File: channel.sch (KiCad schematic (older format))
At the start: 7 parts, among them Q1 MMBT5551, Q2 SiS402DN, Q3 MMBT5401

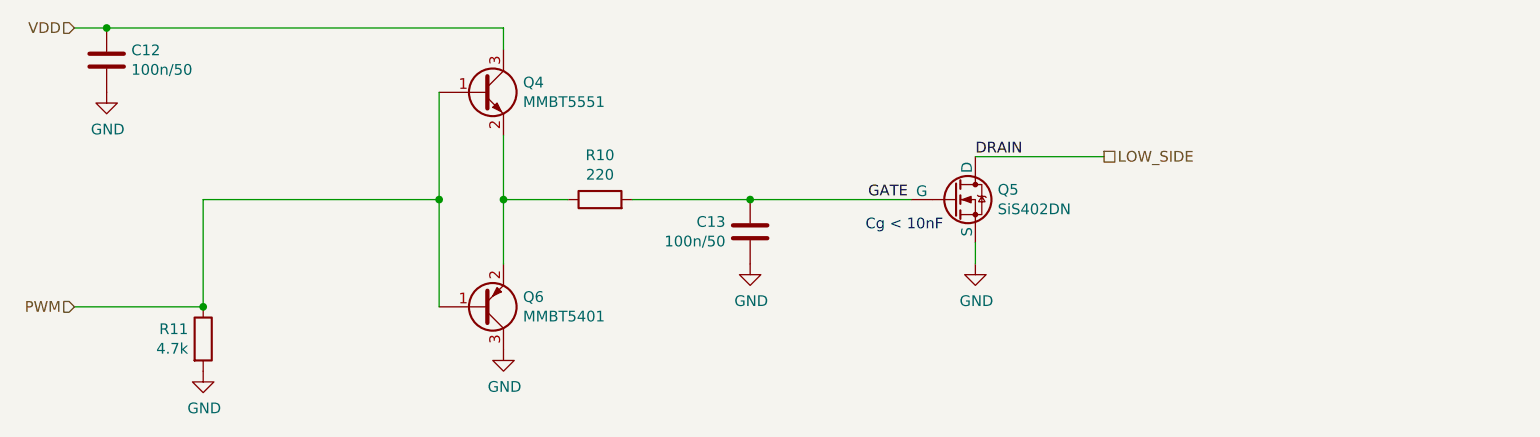
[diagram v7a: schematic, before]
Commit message: add mosfets, fix led+i2c resistors
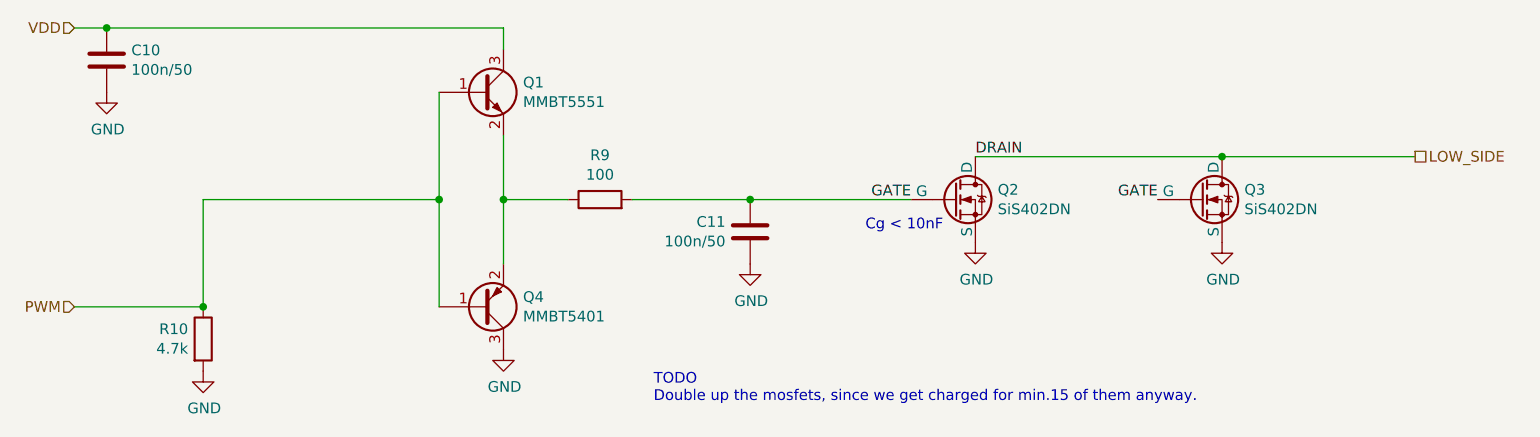
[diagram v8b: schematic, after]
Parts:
- added Q3: SiS402DN, Package_SO:Vishay_PowerPAK_1212-8_Single, symbol mark:SiS402DN
- Q2: JLC (none) -> C15791
- R9: renamed from R8; value 220 -> 100; JLC C25091 -> C25076
- renumbered Q3 to Q4, R9 to R10
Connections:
- net GATE: now also Q3.4 (G)
- net GND: now also Q3.1 (S), Q3.2 (S), Q3.3 (S)
- net LOW_SIDE: now also Q3.5 (D)
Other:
- note added: "TODO\nDouble up the mosfets, since we get charged for min.15 of them anyway."
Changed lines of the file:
@@
 AR Path="/61C031A1/61C0AE1D" Ref="#PWR?"  Part="1"
 AR Path="/61C031A3/61C0AE1D" Ref="#PWR?"  Part="1"
-AR Path="/6202E846/61C0AE1D" Ref="#PWR030"  Part="1"
-AR Path="/620593AE/61C0AE1D" Ref="#PWR035"  Part="1"
-F 0 "#PWR035" H 3000 2400 50  0001 C CNN
+AR Path="/6202E846/61C0AE1D" Ref="#PWR031"  Part="1"
+AR Path="/620593AE/61C0AE1D" Ref="#PWR037"  Part="1"
+F 0 "#PWR031" H 3000 2400 50  0001 C CNN
 F 1 "GND" H 3005 2477 50  0000 C CNN
 F 2 "" H 3000 2650 50  0001 C CNN
@@
 AR Path="/61C031A3/61C0ECF9" Ref="R?"  Part="1"
 AR Path="/61C0ECF9" Ref="R?"  Part="1"
-AR Path="/6202E846/61C0ECF9" Ref="R9"  Part="1"
-AR Path="/620593AE/61C0ECF9" Ref="R11"  Part="1"
-F 0 "R11" H 1530 2646 50  0000 R CNN
+AR Path="/6202E846/61C0ECF9" Ref="R10"  Part="1"
+AR Path="/620593AE/61C0ECF9" Ref="R12"  Part="1"
+F 0 "R10" H 1530 2646 50  0000 R CNN
 F 1 "4.7k" H 1530 2555 50  0000 R CNN
 F 2 "Resistor_SMD:R_0402_1005Metric" V 1530 2600 50  0001 C CNN
@@
 AR Path="/61C031A1/61C1051F" Ref="#PWR?"  Part="1"
 AR Path="/61C031A3/61C1051F" Ref="#PWR?"  Part="1"
-AR Path="/6202E846/61C1051F" Ref="#PWR031"  Part="1"
-AR Path="/620593AE/61C1051F" Ref="#PWR036"  Part="1"
-F 0 "#PWR036" H 1600 2500 50  0001 C CNN
+AR Path="/6202E846/61C1051F" Ref="#PWR032"  Part="1"
+AR Path="/620593AE/61C1051F" Ref="#PWR038"  Part="1"
+F 0 "#PWR032" H 1600 2500 50  0001 C CNN
 F 1 "GND" H 1605 2577 50  0000 C CNN
 F 2 "" H 1600 2750 50  0001 C CNN
@@
 P 2900 1450
 AR Path="/6202E846/61C0A1BB" Ref="Q1"  Part="1"
-AR Path="/620593AE/61C0A1BB" Ref="Q4"  Part="1"
-F 0 "Q4" H 3091 1496 50  0000 L CNN
+AR Path="/620593AE/61C0A1BB" Ref="Q5"  Part="1"
+F 0 "Q1" H 3091 1496 50  0000 L CNN
 F 1 "MMBT5551" H 3091 1405 50  0000 L CNN
 F 2 "Package_TO_SOT_SMD:SOT-23" H 3100 1375 50  0001 L CIN
@@
 AR Path="/61C031A3/61C5A1AF" Ref="R?"  Part="1"
 AR Path="/61C5A1AF" Ref="R?"  Part="1"
-AR Path="/6202E846/61C5A1AF" Ref="R8"  Part="1"
-AR Path="/620593AE/61C5A1AF" Ref="R10"  Part="1"
-F 0 "R10" V 3657 1950 50  0000 C CNN
-F 1 "220" V 3566 1950 50  0000 C CNN
+AR Path="/6202E846/61C5A1AF" Ref="R9"  Part="1"
+AR Path="/620593AE/61C5A1AF" Ref="R11"  Part="1"
+F 0 "R9" V 3657 1950 50  0000 C CNN
+F 1 "100" V 3566 1950 50  0000 C CNN
 F 2 "Resistor_SMD:R_0402_1005Metric_Pad0.72x0.64mm_HandSolder" V 3380 1950 50  0001 C CNN
 F 3 "~" H 3450 1950 50  0001 C CNN
-F 4 "C25091" H 3450 1950 50  0001 C CNN "JLC"
+F 4 "C25076" H 3450 1950 50  0001 C CNN "JLC"
 	1    3450 1950
 	0    -1   -1   0
@@
 	3000 1150 3000 1250
 $Comp
-L Device:Q_PNP_BEC Q3
+L Device:Q_PNP_BEC Q4
 U 1 1 61C4E023
 P 2900 2450
-AR Path="/6202E846/61C4E023" Ref="Q3"  Part="1"
-AR Path="/620593AE/61C4E023" Ref="Q6"  Part="1"
-F 0 "Q6" H 3091 2404 50  0000 L CNN
+AR Path="/6202E846/61C4E023" Ref="Q4"  Part="1"
+AR Path="/620593AE/61C4E023" Ref="Q8"  Part="1"
+F 0 "Q4" H 3091 2404 50  0000 L CNN
 F 1 "MMBT5401" H 3091 2495 50  0000 L CNN
 F 2 "Package_TO_SOT_SMD:SOT-23" H 3100 2550 50  0001 C CNN
@@
 AR Path="/6202E846/61D142B7" Ref="C10"  Part="1"
 AR Path="/620593AE/61D142B7" Ref="C12"  Part="1"
-F 0 "C12" H 1265 1346 50  0000 L CNN
+F 0 "C10" H 1265 1346 50  0000 L CNN
 F 1 "100n/50" H 1265 1255 50  0000 L CNN
 F 2 "Capacitor_SMD:C_0402_1005Metric" H 1188 1150 50  0001 C CNN
@@
 AR Path="/61C031A3/61D15BBF" Ref="#PWR?"  Part="1"
 AR Path="/6202E846/61D15BBF" Ref="#PWR027"  Part="1"
-AR Path="/620593AE/61D15BBF" Ref="#PWR032"  Part="1"
-F 0 "#PWR032" H 1150 1200 50  0001 C CNN
+AR Path="/620593AE/61D15BBF" Ref="#PWR033"  Part="1"
+F 0 "#PWR027" H 1150 1200 50  0001 C CNN
 F 1 "GND" H 1155 1277 50  0000 C CNN
 F 2 "" H 1150 1450 50  0001 C CNN
@@
 	4150 1950 4900 1950
 Wire Wire Line
-	5200 1750 5800 1750
+	5200 1750 6350 1750
 $Comp
 L mark:SiS402DN Q2
@@
 P 5100 1950
 AR Path="/6202E846/622D62B8" Ref="Q2"  Part="1"
-AR Path="/620593AE/622D62B8" Ref="Q5"  Part="1"
-F 0 "Q5" H 5304 1996 50  0000 L CNN
+AR Path="/620593AE/622D62B8" Ref="Q6"  Part="1"
+F 0 "Q2" H 5304 1996 50  0000 L CNN
 F 1 "SiS402DN" H 5304 1905 50  0000 L CNN
 F 2 "Package_SO:Vishay_PowerPAK_1212-8_Single" H 5100 2450 50  0001 C CNN
 F 3 "https://datasheet.lcsc.com/lcsc/1809301517_Vishay-Intertech-SIS402DN-T1-GE3_C15791.pdf" H 5100 1950 50  0001 C CNN
+F 4 "C15791" H 5100 1950 50  0001 C CNN "JLC"
 	1    5100 1950
 	1    0    0    -1
 $EndComp
-Text HLabel 5800 1750 2    50   UnSpc ~ 0
+Text HLabel 7250 1750 2    50   UnSpc ~ 0
 LOW_SIDE
 $Comp
 L power:GND #PWR?
 U 1 1 6203BB32
-P 5200 2250
+P 5200 2150
 AR Path="/61B5C5B6/6203BB32" Ref="#PWR?"  Part="1"
 AR Path="/61C03040/6203BB32" Ref="#PWR?"  Part="1"
@@
 AR Path="/61C031A3/6203BB32" Ref="#PWR?"  Part="1"
 AR Path="/6203BB32" Ref="#PWR?"  Part="1"
-AR Path="/6202E846/6203BB32" Ref="#PWR029"  Part="1"
+AR Path="/6202E846/6203BB32" Ref="#PWR028"  Part="1"
 AR Path="/620593AE/6203BB32" Ref="#PWR034"  Part="1"
-F 0 "#PWR034" H 5200 2000 50  0001 C CNN
-F 1 "GND" H 5205 2077 50  0000 C CNN
-F 2 "" H 5200 2250 50  0001 C CNN
-F 3 "" H 5200 2250 50  0001 C CNN
-	1    5200 2250
+F 0 "#PWR028" H 5200 1900 50  0001 C CNN
+F 1 "GND" H 5205 1977 50  0000 C CNN
+F 2 "" H 5200 2150 50  0001 C CNN
+F 3 "" H 5200 2150 50  0001 C CNN
+	1    5200 2150
 	1    0    0    -1
 $EndComp
 Text Label 5200 1750 0    50   ~ 0
 DRAIN
-Text Label 4700 1950 0    50   ~ 0
+Text Label 4900 1950 2    50   ~ 0
 GATE
-Wire Wire Line
-	5200 2250 5200 2150
 Connection ~ 4150 1950
 Wire Wire Line
@@
 AR Path="/6202E846/61C61D09" Ref="C11"  Part="1"
 AR Path="/620593AE/61C61D09" Ref="C13"  Part="1"
-F 0 "C13" H 4035 2146 50  0000 R CNN
+F 0 "C11" H 4035 2146 50  0000 R CNN
 F 1 "100n/50" H 4035 2055 50  0000 R CNN
 F 2 "Capacitor_SMD:C_0402_1005Metric_Pad0.74x0.62mm_HandSolder" H 4188 1950 50  0001 C CNN
@@
 AR Path="/61C031A1/61C20664" Ref="#PWR?"  Part="1"
 AR Path="/61C031A3/61C20664" Ref="#PWR?"  Part="1"
-AR Path="/6202E846/61C20664" Ref="#PWR028"  Part="1"
-AR Path="/620593AE/61C20664" Ref="#PWR033"  Part="1"
-F 0 "#PWR033" H 4150 2000 50  0001 C CNN
+AR Path="/6202E846/61C20664" Ref="#PWR030"  Part="1"
+AR Path="/620593AE/61C20664" Ref="#PWR036"  Part="1"
+F 0 "#PWR030" H 4150 2000 50  0001 C CNN
 F 1 "GND" H 4155 2077 50  0000 C CNN
 F 2 "" H 4150 2250 50  0001 C CNN
@@
 	1    0    0    -1
 $EndComp
+Text Notes 3700 2900 0    50   ~ 0
+TODO\nDouble up the mosfets, since we get charged for min.15 of them anyway.
+$Comp
+L mark:SiS402DN Q3
+U 1 1 6236D64F
+P 6250 1950
+AR Path="/6202E846/6236D64F" Ref="Q3"  Part="1"
+AR Path="/620593AE/6236D64F" Ref="Q7"  Part="1"
+F 0 "Q3" H 6454 1996 50  0000 L CNN
+F 1 "SiS402DN" H 6454 1905 50  0000 L CNN
+F 2 "Package_SO:Vishay_PowerPAK_1212-8_Single" H 6250 2450 50  0001 C CNN
+F 3 "https://datasheet.lcsc.com/lcsc/1809301517_Vishay-Intertech-SIS402DN-T1-GE3_C15791.pdf" H 6250 1950 50  0001 C CNN
+F 4 "C15791" H 6250 1950 50  0001 C CNN "JLC"
+	1    6250 1950
+	1    0    0    -1
+$EndComp
+Connection ~ 6350 1750
+Wire Wire Line
+	6350 1750 7250 1750
+Text Label 6050 1950 2    50   ~ 0
+GATE
+$Comp
+L power:GND #PWR?
+U 1 1 6236E79F
+P 6350 2150
+AR Path="/61B5C5B6/6236E79F" Ref="#PWR?"  Part="1"
+AR Path="/61C03040/6236E79F" Ref="#PWR?"  Part="1"
+AR Path="/61C031A1/6236E79F" Ref="#PWR?"  Part="1"
+AR Path="/61C031A3/6236E79F" Ref="#PWR?"  Part="1"
+AR Path="/6236E79F" Ref="#PWR?"  Part="1"
+AR Path="/6202E846/6236E79F" Ref="#PWR029"  Part="1"
+AR Path="/620593AE/6236E79F" Ref="#PWR035"  Part="1"
+F 0 "#PWR029" H 6350 1900 50  0001 C CNN
+F 1 "GND" H 6355 1977 50  0000 C CNN
+F 2 "" H 6350 2150 50  0001 C CNN
+F 3 "" H 6350 2150 50  0001 C CNN
+	1    6350 2150
+	1    0    0    -1
+$EndComp
